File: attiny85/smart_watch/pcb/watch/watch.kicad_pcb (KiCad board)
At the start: 2 copper layers, 5 parts, among them J1 Conn_01x04_Pin, SW1 Wake, SW2 Select, SW3 Set, U1 ATTINY85

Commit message: PCB mounting
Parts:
- added BT1: Battery_Cell, Battery:BatteryHolder_Keystone_1058_1x2032, B.Cu at (151.1, 90.2)
- added C1: 4.7uF, Capacitor_SMD:C_0805_2012Metric, F.Cu at (163.9, 93.2)
- added C2: 4.7uF, Capacitor_SMD:C_0805_2012Metric, F.Cu at (163.8, 90.6)
- added H1: MountingHole, MountingHole:MountingHole_2.1mm, F.Cu at (125.7, 68.5)
- added H2: MountingHole, MountingHole:MountingHole_2.1mm, F.Cu at (125.7, 101.0)
- added H3: MountingHole, MountingHole:MountingHole_2.1mm, F.Cu at (164.8, 100.7)
- added H4: MountingHole, MountingHole:MountingHole_2.1mm, F.Cu at (165.2, 68.3)
- added J2: USB C, Connector_USB:USB_C_Receptacle_HRO_TYPE-C-31-M-17, F.Cu at (156.7, 69.4)
- added LED1: Charger LED, LED_SMD:LED_0805_2012Metric_Pad1.15x1.40mm_HandSolder, F.Cu at (130.6, 100.8)
- added R1: 5.1k, Resistor_SMD:R_0805_2012Metric, F.Cu at (163.9, 80.4)
- added R2: 5.1k, Resistor_SMD:R_0805_2012Metric, F.Cu at (164.0, 82.8)
- added R3: 3.6k, Resistor_SMD:R_0805_2012Metric, F.Cu at (164.0, 85.5)
- added R4: 470, Resistor_SMD:R_0805_2012Metric, F.Cu at (163.8, 88.0)
- added SW4: Reset, Button_Switch_THT:SW_TH_Tactile_Omron_B3F-100x, F.Cu at (134.5, 67.9)
- added U2: MCP73831-2-OT, Package_TO_SOT_SMD:SOT-23-5, F.Cu at (164.3, 76.6)
- J1: value Conn_01x04_Pin -> Display
- moved J1 21.6 mm to (142.2, 77.5)
- moved U1 18.1 mm to (124.3, 88.9)
- moved SW1 17.6 mm to (143.5, 67.9)
- moved SW3 16.9 mm to (125.1, 81.7)
- moved SW2 13.0 mm to (125.1, 74.3)
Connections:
- net Select renamed SELECT
- net Set renamed SET
- net Wake renamed WAKE
- U1 pad 1: unconnected-(U1-~{RESET}/PB5-Pad1) -> RESET
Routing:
- net VBUS: track 0.00 -> 65.7 mm, vias 0 -> 2
- net VCC: track 0.00 -> 65.0 mm, vias 0 -> 4
- net Net-(LED1-K): track 0.00 -> 38.6 mm
- net WAKE: track 0.00 -> 35.3 mm
- net SDA: track 0.00 -> 27.8 mm
- net RESET: track 0.00 -> 27.2 mm
- net SELECT: track 0.00 -> 23.1 mm
- net SCK: track 0.00 -> 21.2 mm
- net SET: track 0.00 -> 17.5 mm
- net Net-(J2-CC2): track 0.00 -> 13.1 mm
- net Net-(U2-STAT): track 0.00 -> 11.7 mm
- net Net-(J2-CC1): track 0.00 -> 10.2 mm
- net Net-(U2-PROG): track 0.00 -> 8.64 mm
- net GND: vias 0 -> 1
- added copper zone on B.Cu, net GND
- added copper zone on F.Cu, net GND
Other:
- board outline added: 45.2 x 38.6 mm

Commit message: production files
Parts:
- added J3: LiPo Batt, Connector_JST:JST_PH_S2B-PH-K_1x02_P2.00mm_Horizontal, B.Cu at (135.1, 79.6)
- BT1: value Battery_Cell -> 1059; footprint Battery:BatteryHolder_Keystone_1058_1x2032 -> BatteryHolder_Keystone_1059_THT:BatteryHolder_Keystone_1059_THT
- moved BT1 3.30 mm to (147.8, 90.2)
- moved SW1 1.44 mm to (144.3, 66.7)
- moved SW4 1.44 mm to (135.3, 66.7)
- moved SW3 0.99 mm to (124.2, 81.2)
- moved SW2 0.99 mm to (124.3, 73.8)
- moved J2 0.76 mm to (157.5, 69.5)
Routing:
- net VCC: track 65.0 -> 79.2 mm, vias 4 -> 0
- net Net-(LED1-K): track 38.6 -> 47.5 mm
- net VBUS: track 65.7 -> 68.7 mm
- net SET: track 17.5 -> 15.7 mm
- net RESET: track 27.2 -> 28.7 mm
- net SDA: track 27.8 -> 26.5 mm
- net SCK: track 21.2 -> 22.2 mm
- net SELECT: track 23.1 -> 22.3 mm
- net Net-(U2-STAT): track 11.7 -> 11.0 mm
- net WAKE: track 35.3 -> 34.7 mm

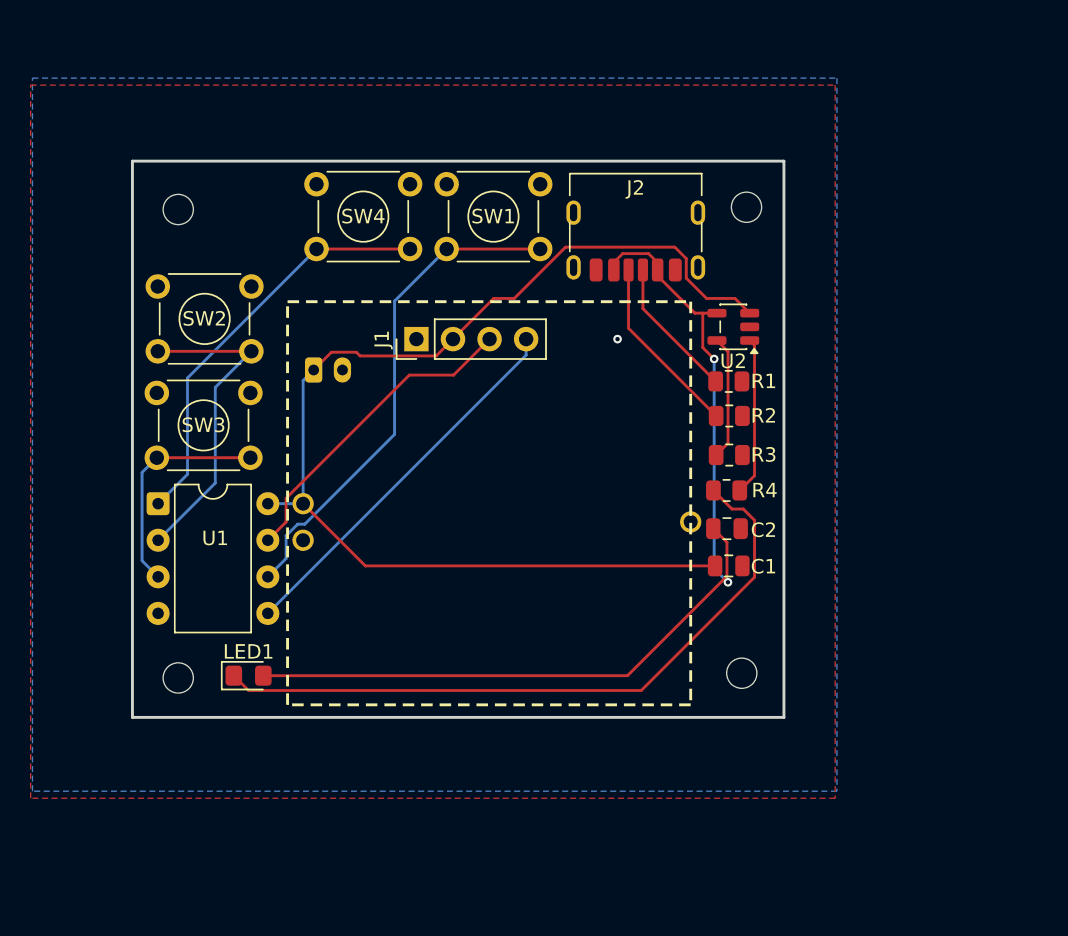
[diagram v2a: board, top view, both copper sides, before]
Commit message: added programming connection
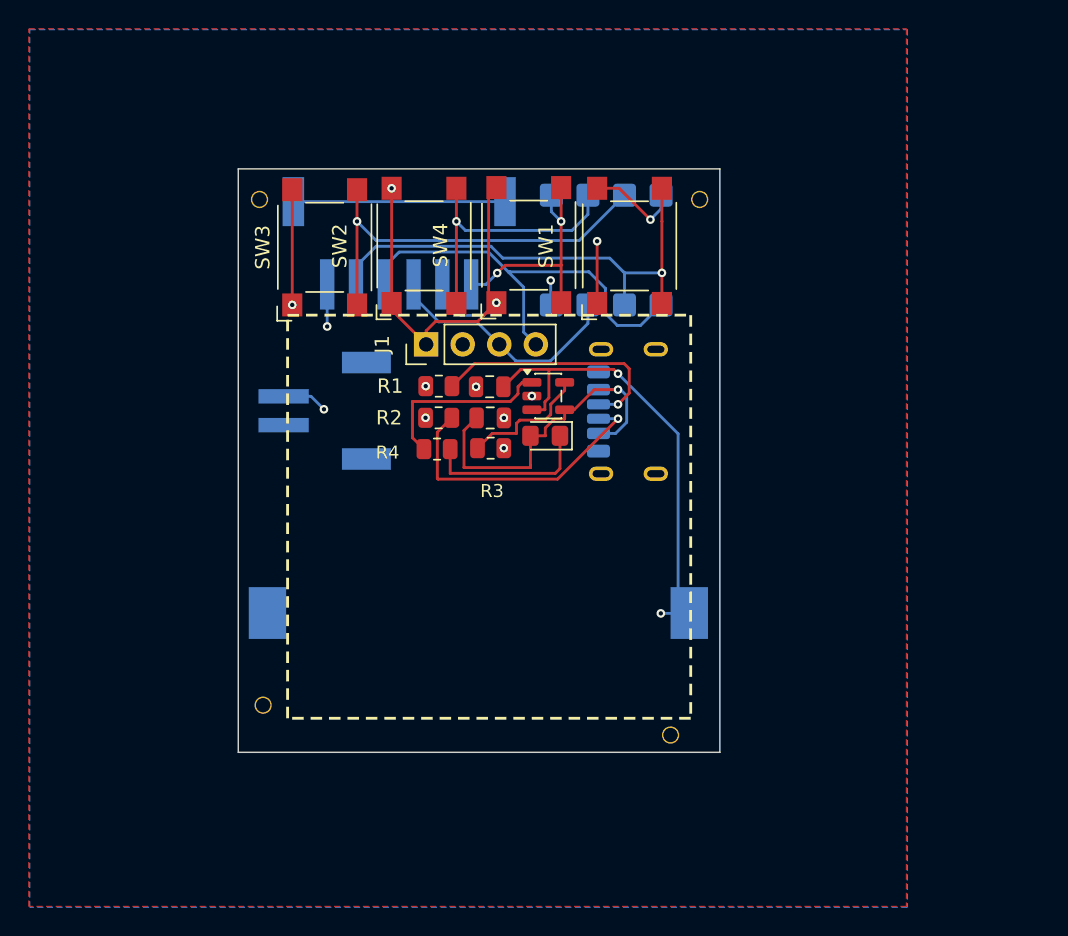
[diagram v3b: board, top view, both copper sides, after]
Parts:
- removed H1, H2, H3: MountingHole, MountingHole:MountingHole_2.1mm
- added H4: MountingHole, MountingHole:MountingHole_2.1mm, F.Cu at (131.6, 102.9)
- added H4: MountingHole, MountingHole:MountingHole_2.1mm, F.Cu at (131.3, 67.8)
- added H4: MountingHole, MountingHole:MountingHole_2.1mm, F.Cu at (159.9, 105.0)
- added P1: JST_LIPO, JST_PH_1x02_2mm_horizontal:JST_PH_1x02_2mm_horizontal, B.Cu at (133.0, 82.4)
- BT1: value 1059 -> Battery_Cell; footprint BatteryHolder_Keystone_1059_THT:BatteryHolder_Keystone_1059_THT -> Battery:BatteryHolder_Keystone_1060_1x2032
- J2: moved to B.Cu
- J3: value LiPo Batt -> Programmer; footprint Connector_JST:JST_PH_S2B-PH-K_1x02_P2.00mm_Horizontal -> JST_PH_1x06_2mm_horizontal:JST_PH_1x06_2mm_horizontal.pretty
- R3: value 3.6k -> 6.8k
- SW1, SW2, SW3, SW4: footprint Button_Switch_THT:SW_TH_Tactile_Omron_B3F-100x -> Button_Switch_SMD:SW_SPST_Omron_B3FS-101xP
- U1: footprint Package_DIP:DIP-8_W7.62mm -> Package_DIP:DIP-8_W7.62mm_SMDSocket_SmallPads; moved to B.Cu
- moved U1 35.8 mm to (155.4, 71.3), turned to -90 degrees
- moved LED1 26.5 mm to (151.2, 84.2), turned to 180 degrees
- moved C1 20.8 mm to (147.3, 80.8), turned to 180 degrees
- moved R4 20.3 mm to (143.7, 85.1), turned to 180 degrees
- moved R2 20.2 mm to (143.8, 82.9), turned to 180 degrees
- moved R1 20.1 mm to (143.8, 80.7), turned to 180 degrees
- moved SW2 18.7 mm to (142.8, 71.0), turned to 90 degrees
- moved C2 18.2 mm to (147.4, 82.9)
- moved R3 16.6 mm to (147.4, 85.0)
- moved SW3 15.4 mm to (135.9, 71.1), turned to 90 degrees
- moved SW4 15.3 mm to (150.0, 70.9), turned to 90 degrees
- moved U2 13.7 mm to (151.4, 81.4), turned to 0 degrees
- moved SW1 13.4 mm to (157.0, 71.0), turned to 90 degrees
- moved J2 13.0 mm to (158.1, 82.5), turned to -90 degrees
- moved J3 8.40 mm to (141.0, 73.7)
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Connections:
- J1 pad 4: SDA -> MOSI
- J3 pad 2: GND -> MISO
- SW1 pad 2: WAKE -> MISO
- U1 pad 5: SDA -> MOSI
- U1 pad 6: WAKE -> MISO
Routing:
- net GND: track 0.00 -> 51.3 mm, vias 1 -> 11
- net VBUS: track 68.7 -> 25.4 mm, vias 2 -> 1
- net VCC: track 79.2 -> 39.4 mm, vias 0 -> 5
- net Net-(LED1-K): track 47.5 -> 11.7 mm
- net WAKE: track 34.7 -> 0.00 mm
- net MISO: track 0.00 -> 34.1 mm, vias 0 -> 1
- net MOSI: track 0.00 -> 30.4 mm
- net SDA: track 26.5 -> 0.00 mm
- net Net-(J3-SHIELD-PadS1): track 0.00 -> 14.7 mm
- net SET: track 15.7 -> 28.4 mm, vias 0 -> 1
- net RESET: track 28.7 -> 16.9 mm, vias 0 -> 2
- net Net-(J2-CC2): track 12.7 -> 20.4 mm, vias 0 -> 1
- net Net-(J2-CC1): track 9.83 -> 17.3 mm, vias 0 -> 1
- net SCK: track 22.2 -> 17.2 mm
- net SELECT: track 22.3 -> 19.2 mm, vias 0 -> 1
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- added copper zone on F.Cu, net VCC
- removed copper zone on F.Cu, net GND
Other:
- board size 45.2 x 38.6 mm -> 33.5 x 40.5 mm

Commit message: watch with straps
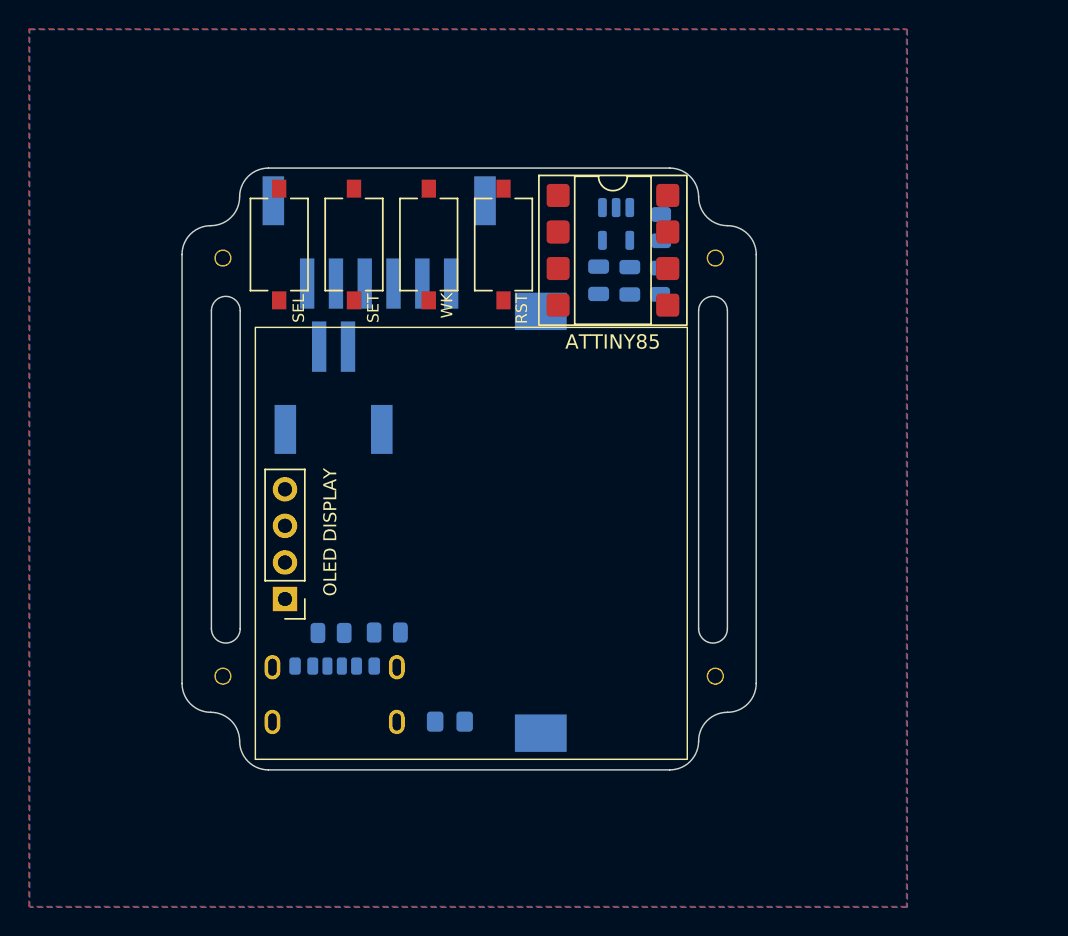
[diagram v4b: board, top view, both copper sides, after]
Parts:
- removed the H4 at (131.6, 102.9)
- removed the H4 at (131.3, 67.8)
- removed the H4 at (161.9, 67.8)
- removed the H4 at (159.9, 105.0)
- removed J1: Display, Connector_PinHeader_2.54mm:PinHeader_1x04_P2.54mm_Vertical
- added H1: MountingHole, My_Footprints:Circular_Mounting_Hole_1mmDia, F.Cu at (128.8, 71.8)
- added H2: MountingHole, My_Footprints:Circular_Mounting_Hole_1mmDia, F.Cu at (128.8, 100.9)
- added H3: MountingHole, My_Footprints:Circular_Mounting_Hole_1mmDia, F.Cu at (163.0, 71.8)
- added H4: MountingHole, My_Footprints:Circular_Mounting_Hole_1mmDia, F.Cu at (163.0, 100.9)
- added OLED DISPLAY: SSD1306_OLED_Display_128x64, My_Footprints:SSD1306_OLED_Display_128x64, F.Cu at (130.6, 91.7)
- ATTINY85: renamed from U1; moved to F.Cu
- C1, C2, LED1, R1, R2, R3, R4, U2: moved to B.Cu
- RST: renamed from SW4; footprint Button_Switch_SMD:SW_SPST_Omron_B3FS-101xP -> Button_Switch_SMD:SW_Tactile_SPST_NO_Straight_CK_PTS636Sx25SMTRLFS
- SEL: renamed from SW2; footprint Button_Switch_SMD:SW_SPST_Omron_B3FS-101xP -> Button_Switch_SMD:SW_Tactile_SPST_NO_Straight_CK_PTS636Sx25SMTRLFS
- SET: renamed from SW3; footprint Button_Switch_SMD:SW_SPST_Omron_B3FS-101xP -> Button_Switch_SMD:SW_Tactile_SPST_NO_Straight_CK_PTS636Sx25SMTRLFS
- USBC: renamed from J2; footprint Connector_USB:USB_C_Receptacle_HRO_TYPE-C-31-M-17 -> Connector_USB:USB_C_Receptacle_GCT_USB4125-xx-x-0190_6P_TopMnt_Horizontal
- WK: renamed from SW1; footprint Button_Switch_SMD:SW_SPST_Omron_B3FS-101xP -> Button_Switch_SMD:SW_Tactile_SPST_NO_Straight_CK_PTS636Sx25SMTRLFS
- moved USBC 29.9 mm to (136.6, 103.3), turned to 180 degrees
- moved R4 21.9 mm to (159.2, 69.7), turned to 90 degrees
- moved LED1 20.9 mm to (144.6, 104.0), turned to 0 degrees
- moved R1 17.5 mm to (140.2, 97.8)
- moved R2 16.7 mm to (136.3, 97.9)
- moved R3 16.5 mm to (159.2, 73.4), turned to 90 degrees
- moved WK 13.9 mm to (143.1, 70.9)
- moved C2 13.6 mm to (157.1, 73.4), turned to -90 degrees
- moved U2 12.8 mm to (156.1, 69.5), turned to -90 degrees
- moved C1 10.6 mm to (154.9, 73.4), turned to 90 degrees
- moved SEL 10.1 mm to (132.7, 70.9)
- moved BT1 7.65 mm to (150.9, 90.2), turned to -90 degrees
- moved P1 5.65 mm to (136.5, 78.0), turned to 0 degrees
- moved SET 2.05 mm to (137.9, 70.9)
- moved RST 1.75 mm to (148.3, 70.9)
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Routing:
- net GND: track 51.3 -> 0.00 mm, vias 11 -> 0
- net VCC: track 39.4 -> 0.00 mm, vias 5 -> 0
- net MISO: track 34.1 -> 0.00 mm, vias 1 -> 0
- net MOSI: track 30.4 -> 0.00 mm
- net SET: track 28.4 -> 0.00 mm, vias 1 -> 0
- net VBUS: track 25.4 -> 0.00 mm, vias 1 -> 0
- net Net-(J2-CC2): track 20.4 -> 0.00 mm, vias 1 -> 0
- net SELECT: track 19.2 -> 0.00 mm, vias 1 -> 0
- net Net-(J2-CC1): track 17.3 -> 0.00 mm, vias 1 -> 0
- net SCK: track 17.2 -> 0.00 mm
- net RESET: track 16.9 -> 0.00 mm, vias 2 -> 0
- net Net-(J3-SHIELD-PadS1): track 14.7 -> 0.00 mm
- net Net-(U2-STAT): track 12.8 -> 0.00 mm
- net Net-(LED1-K): track 11.7 -> 0.00 mm
- net Net-(U2-PROG): track 9.09 -> 0.00 mm
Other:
- board size 33.5 x 40.5 mm -> 39.9 x 41.8 mm
